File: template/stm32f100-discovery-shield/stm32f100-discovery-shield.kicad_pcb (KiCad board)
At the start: 2 copper layers, 3 parts, among them P1 CONN28, P2 CONN28, P3 CONN6

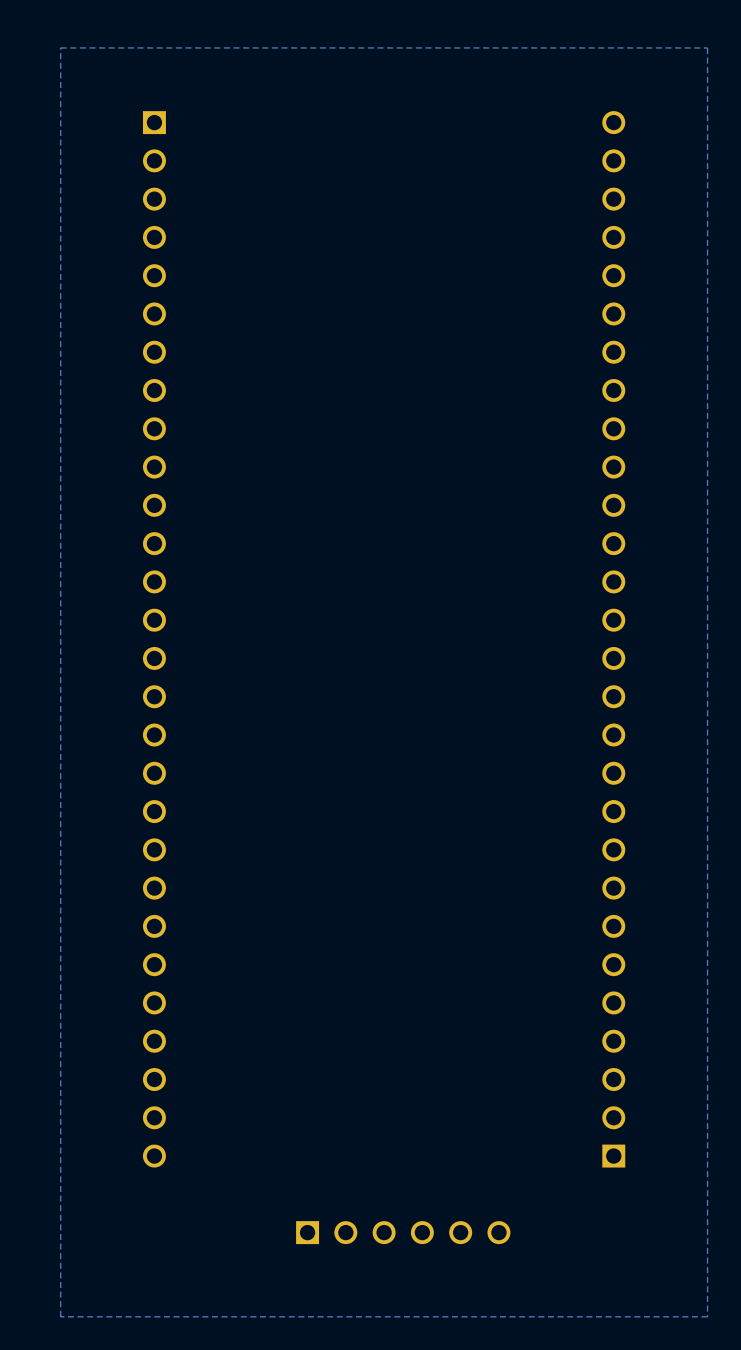
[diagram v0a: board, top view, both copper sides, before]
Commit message: fix #252: template layers translated
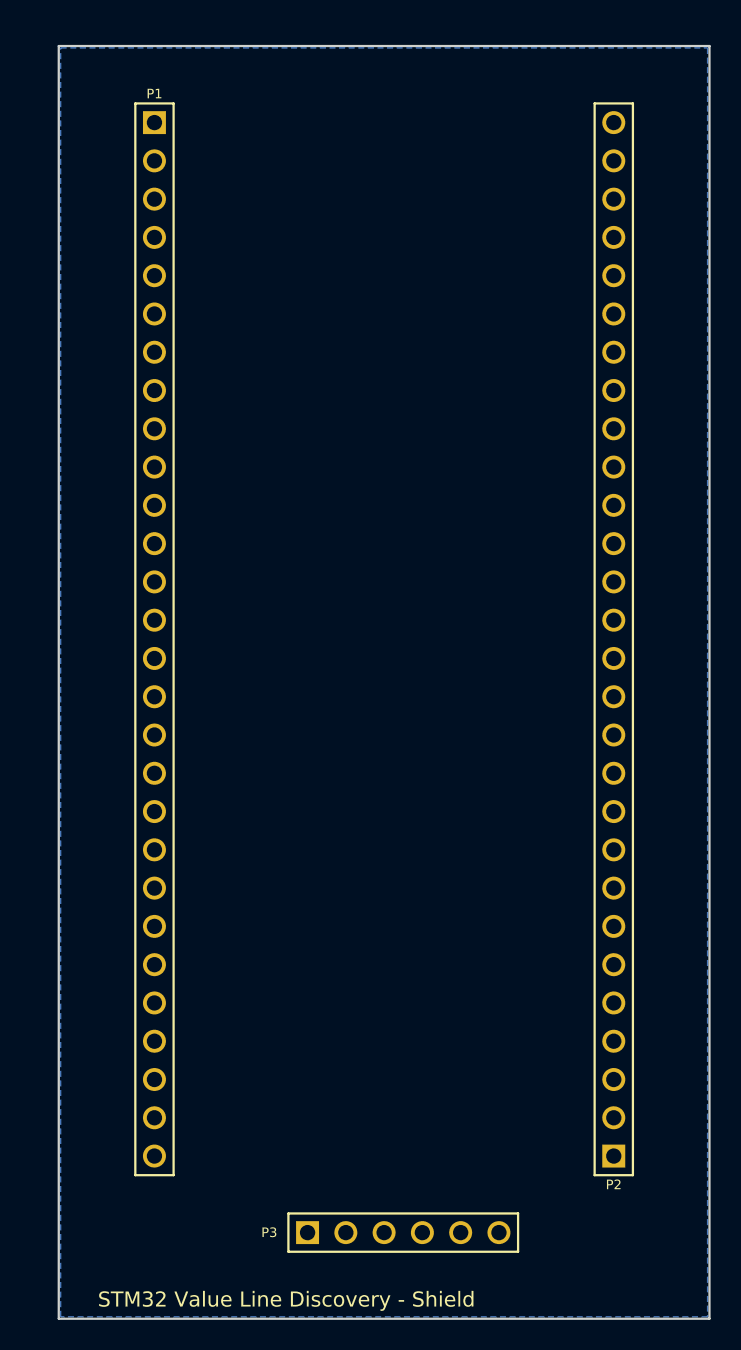
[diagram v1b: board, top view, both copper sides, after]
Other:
- board outline added: 43.2 x 84.5 mm

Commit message: fix template
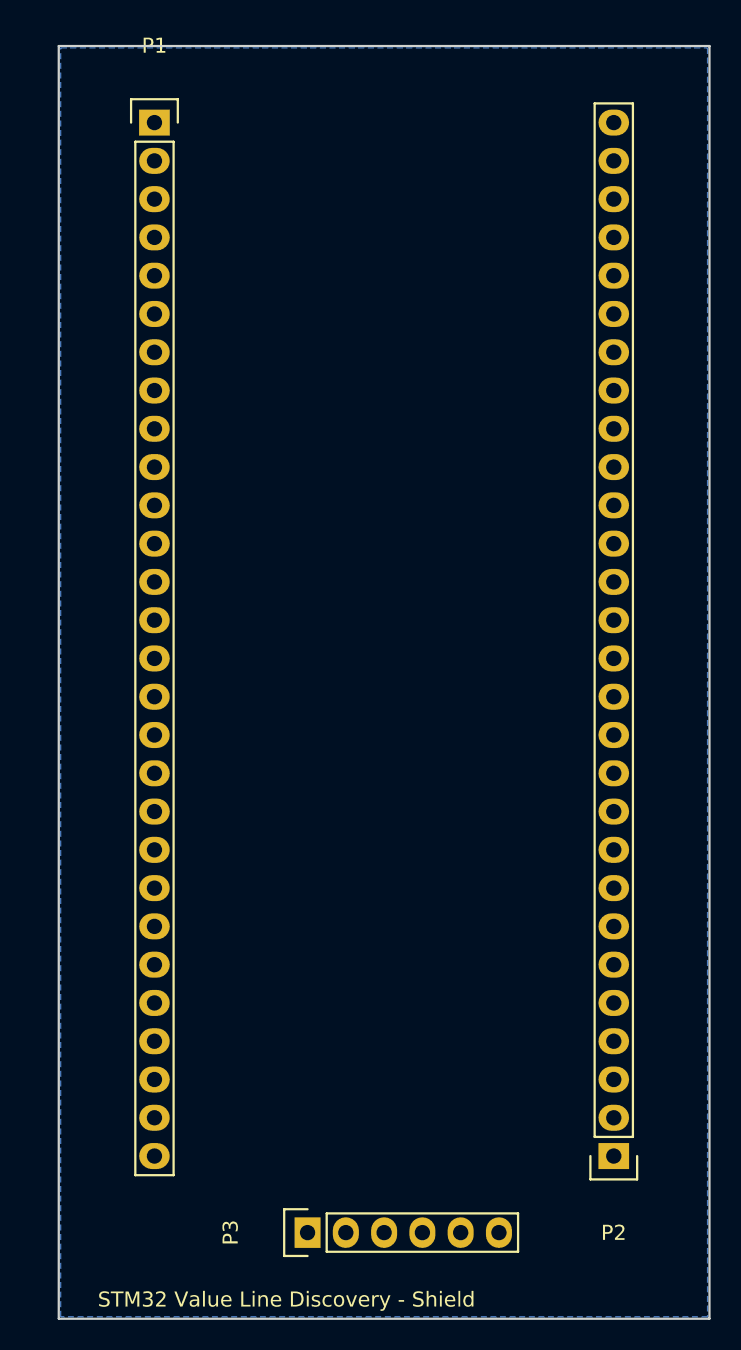
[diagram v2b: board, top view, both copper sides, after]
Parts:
- P1, P2: footprint PIN_ARRAY_28X1 -> Pin_Headers:Pin_Header_Straight_1x28
- P3: footprint PIN_ARRAY_6X1 -> Pin_Headers:Pin_Header_Straight_1x06
- moved P2 34.3 mm to (69.8, 108.0), turned to 180 degrees
- moved P1 34.3 mm to (39.4, 39.4), turned to 0 degrees
- moved P3 6.35 mm to (49.5, 113.0), turned to 90 degrees
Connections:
- P1 pad 3: +3.3V -> (no net)
- P2 pad 26: +5V -> (no net)
